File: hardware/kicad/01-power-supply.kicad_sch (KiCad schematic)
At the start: 8 parts, among them J1 USB_C, U2 IP5306 USB-C, U3 AMS1117-3.3

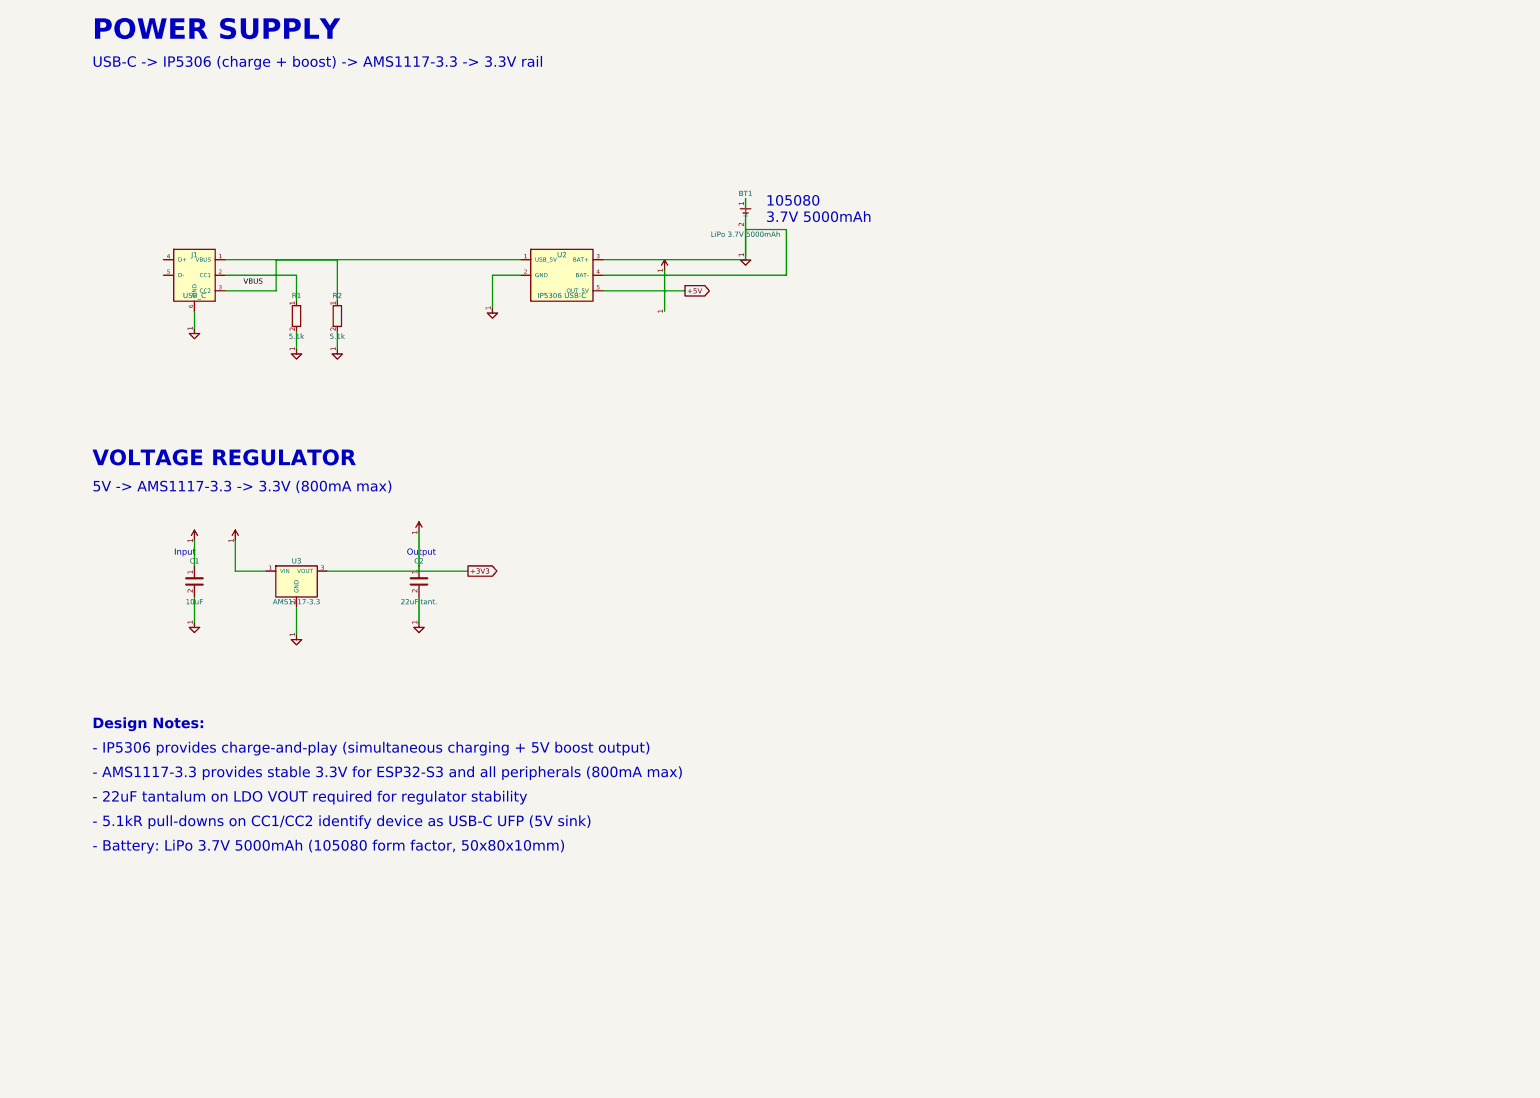
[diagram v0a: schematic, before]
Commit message: Add PCB layout, hierarchical schematics, verification & rendering pipeline
- Reorganize passive components into centered rows below ESP32
- Add missing schematic symbols (LED, FPC_16P, SW_PWR, SW13, SPK1)
- Generate hierarchical root schematic with 7 sub-sheet references
- Create PCB layout generator (4-layer, 160x75mm, JLCPCB-ready)
- Add JLCPCB export (BOM.csv + CPL.csv for 65 components)
- Add schematic/PCB/JLCPCB consistency verification script
- Add PCB SVG renderer + PNG/GIF animation pipeline
- Add interactive 3D PCB viewer (Three.js)
- Update docs (pcb.md, components.md, README.md)

Co-Authored-By: Claude Opus 4.6 <noreply@anthropic.com>
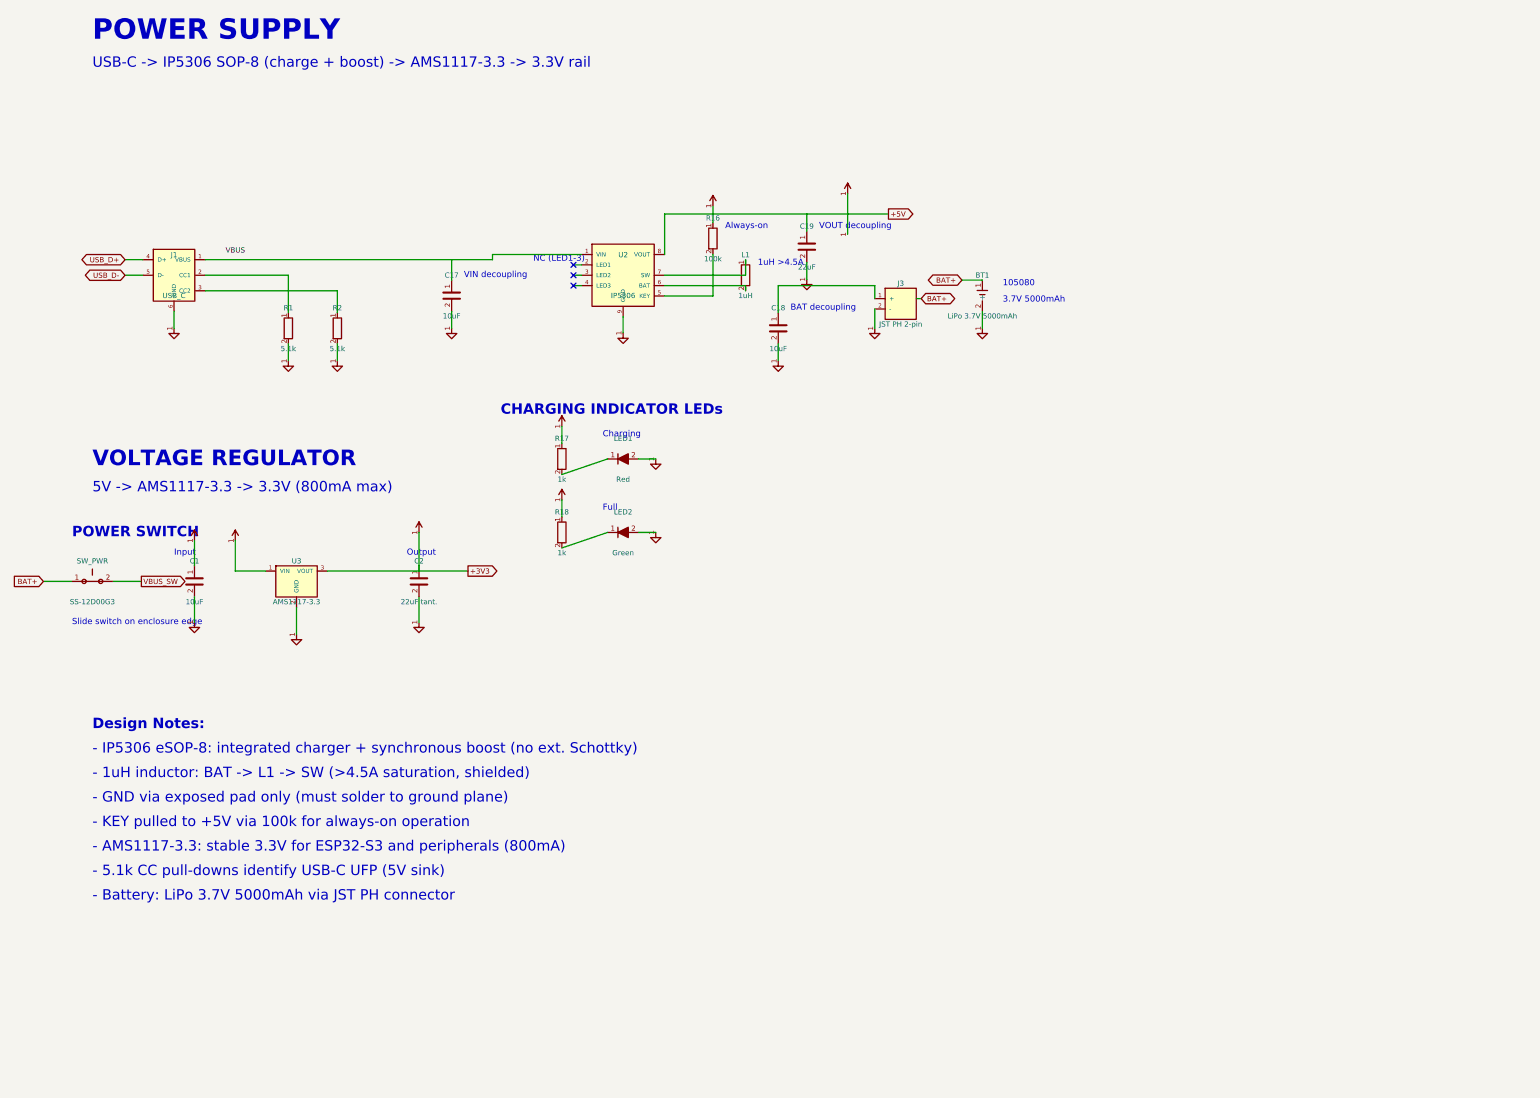
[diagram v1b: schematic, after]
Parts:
- added C17, C18: 10uF, symbol C
- added C19: 22uF, symbol C
- added J3: JST PH 2-pin, symbol Conn_JST_PH_2
- added L1: 1uH, symbol L
- added LED1: Red, symbol LED
- added LED2: Green, symbol LED
- added R16: 100k, symbol R
- added R17, R18: 1k, symbol R
- added SW_PWR: SS-12D00G3, symbol SW_Push
- U2: value IP5306 USB-C -> IP5306; symbol IP5306_Module -> IP5306
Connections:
- net +5V: now also U2.8 (VOUT); no longer U2.5 (OUT_5V)
- net at J1.1 (VBUS), U2.1 (VIN): now also C17.1; no longer J1.3 (CC2), R2.1
- net USB_D+: now reaches J1.4 (D+)
- net USB_D-: now reaches J1.5 (D-)
- new net: J1.3 (CC2), R2.1
- new net: R16.2, U2.5 (KEY)
- new net: L1.2, U2.6 (BAT)
- new net: L1.1, U2.7 (SW)
- new net: C18.1, J3.1 (+)
- new net: LED1.1 (A), R17.2
- new net: LED2.1 (A), R18.2
- new net BAT+: BT1.1 (+), SW_PWR.1
- new net VBUS_SW: SW_PWR.2
- now unconnected: BT1.2 (-), U2.3 (BAT+), U2.4 (BAT-)
- no-connect marks 0 -> 3
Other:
- note added: "- 1uH inductor: BAT -> L1 -> SW (>4.5A saturation, shielded)"
- note added: "- 5.1k CC pull-downs identify USB-C UFP (5V sink)"
- note added: "- AMS1117-3.3: stable 3.3V for ESP32-S3 and peripherals (800mA)"
- note added: "- Battery: LiPo 3.7V 5000mAh via JST PH connector"
- note added: "- GND via exposed pad only (must solder to ground plane)"
- note added: "- IP5306 eSOP-8: integrated charger + synchronous boost (no ext. Schottky)"
- note added: "- KEY pulled to +5V via 100k for always-on operation"
- note added: "1uH >4.5A"
- note added: "Always-on"
- note added: "BAT decoupling"
- note added: "CHARGING INDICATOR LEDs"
- note added: "Charging"
- note added: "Full"
- note added: "NC (LED1-3)"
- note added: "POWER SWITCH"
- note added: "Slide switch on enclosure edge"
- note added: "USB-C -> IP5306 SOP-8 (charge + boost) -> AMS1117-3.3 -> 3.3V rail"
- note added: "VIN decoupling"
- note added: "VOUT decoupling"
- note removed: "- 22uF tantalum on LDO VOUT required for regulator stability"
- note removed: "- 5.1kR pull-downs on CC1/CC2 identify device as USB-C UFP (5V sink)"
- note removed: "- AMS1117-3.3 provides stable 3.3V for ESP32-S3 and all peripherals (800mA max)"
- note removed: "- Battery: LiPo 3.7V 5000mAh (105080 form factor, 50x80x10mm)"
- note removed: "- IP5306 provides charge-and-play (simultaneous charging + 5V boost output)"
- note removed: "USB-C -> IP5306 (charge + boost) -> AMS1117-3.3 -> 3.3V rail"
- moved on the sheet: J1

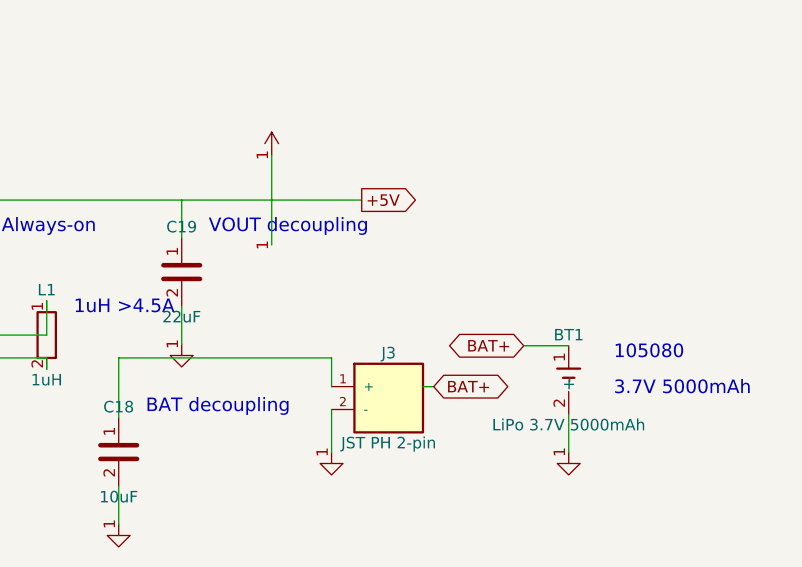
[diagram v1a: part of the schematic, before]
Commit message: feat(pcb): add bypass caps C26/C27, fix USB D+/D- matching, improve DRC/connectivity checks
- Add C26 (100nF VDD bypass near ESP32 pin 2) and C27 (10uF HF decoupling near AMS1117)
- Fix USB D+/D- length mismatch: 5-loop meander (0.46mm amp) reduces delta from 1.75mm to 0.03mm
- Fix LCD_RD/LCD_BL traces to use correct net IDs instead of +3V3
- Improve net connectivity check: count vias, allow stub-to-via patterns, exclude I2S unrouted nets
- Rewrite FPC/ESP32 pin position tests to use routing._PADS as source of truth
- Add Quantity column to BOM for JLCPCB assembly quoting
- Reduce min via hole size 0.3mm→0.2mm in design rules
- All 149 DFM/DFA/JLCPCB tests pass, 0 collisions

Co-Authored-By: Claude Opus 4.6 (1M context) <noreply@anthropic.com>
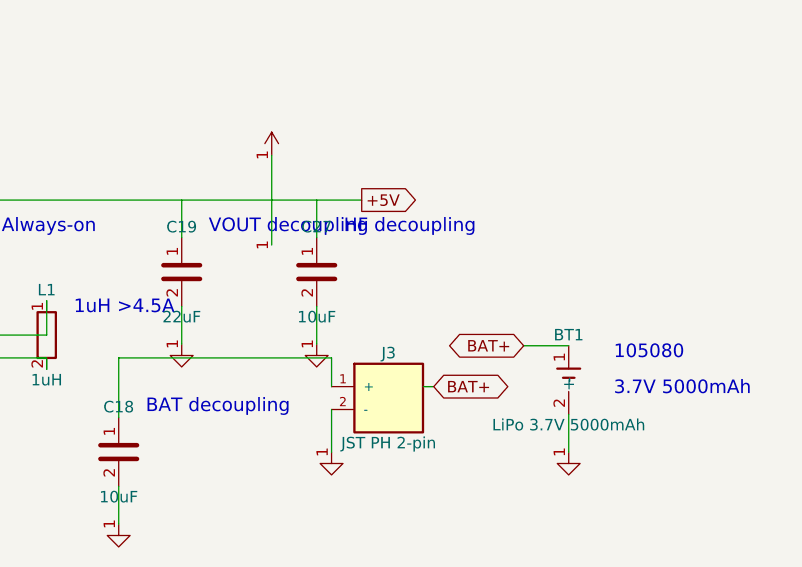
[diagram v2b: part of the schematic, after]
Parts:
- removed C18: 10uF, symbol C
- removed SW_PWR: SS-12D00G3, symbol SW_Push
- added C27: 10uF, symbol C
- added R16: 100k, symbol R
- added R17: 1k, symbol R
- C18: renamed from R16; value 100k -> 10uF; symbol R -> C
- SW_PWR: renamed from R17; value 1k -> SS-12D00G3; symbol R -> SW_Push
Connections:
- net BAT+: now also SW_PWR.1
- net VBUS_SW: now also SW_PWR.2
- net at U2.5 (KEY): now also R16.2; no longer C18.2
- net at J3.1 (+): now also C18.1
- net at LED1.1 (A): now also R17.2; no longer SW_PWR.2
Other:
- note added: "HF decoupling"

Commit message: fix(hw): R4 audit — schematic↔PCB sync guard + 4 fixes + R4-CRIT-1 false-positive closure
Round 4 of the hardware audit found four real schematic/PCB drift bugs
that rounds 1-3 missed because no check cross-validated the two Python
generators. A fifth finding (R4-CRIT-1, "FPC pinout mismatch") turned
out to be a FALSE POSITIVE caused by the landscape FPC pin reversal
(connector_pad = 41 − panel_pin) — verified programmatically against
all 40 J4 pads of the panel datasheet in components.md.

Fixes applied:
  R4-HIGH-1  USBLC6 (U4) + R22/R23 instantiated in power_supply.py —
             previously only in routing.py, invisible to schematic
             review.
  R4-HIGH-2  Display module symbol ref renamed U4 → DS1 in display.py.
             U4 is now cleanly owned by the physical USBLC6 TVS.
  R4-HIGH-3  PAM8403 R20/R21 input bias moved from GND to VREF
             (pin 8) per the datasheet single-ended app circuit.
  R4-CRIT-1  CLOSED as false positive. Both display.py (panel-side)
             and datasheet_specs.py (connector-side) were correct all
             along. Added 41-N reversal documentation at the top of
             both files so the mistake can't be re-raised.
  ERC CRIT   Pre-existing "Power output ↔ Power output" on +5V was
             PWR_FLAG duplicating IP5306 VOUT (already power_out in the
             library symbol). Removed the PWR_FLAG. ERC now 0 critical.

Incidental cleanups required by the new sync guard:
  - mcu.py R3 (external EN pull-up) removed from schematic — already
    DNP in BOM because the WROOM-1 module has an internal pull-up.
  - controls.py D1 BAT54C (MENU combo diode) instantiated in schematic
    to match the PCB routing. MENU button wiring simplified to the
    MENU_K node; there is no dedicated BTN_MENU GPIO (firmware detects
    START+SELECT combo).
  - power_supply.py USB_CC1 / USB_CC2 global labels added so the
    connector-net coverage check sees the full USB-C net set.
  - display.py docstring expanded with the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
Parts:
- removed C18: 10uF, symbol C
- removed C2: 22uF tant., symbol C
- added R1: 5.1k, symbol R
- added R18: 1k, symbol R
- added R22, R23: 22, symbol R
- added SW_PWR: SS-12D00G3, symbol SW_Push
- C1: renamed from SW_PWR; value SS-12D00G3 -> 10uF; symbol SW_Push -> C
- C2: renamed from R18; value 1k -> 22uF tant.; symbol R -> C
- U4: renamed from R1; value 5.1k -> USBLC6-2SC6; symbol R -> USBLC6_2SC6
- renumbered C1 to C18
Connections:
- net +3V3: now also C2.1
- net BAT+: now also SW_PWR.1; no longer C1.1
- net VBUS_SW: now also SW_PWR.2; no longer C1.2
- net USB_CC1: now reaches J1.2 (CC1)
- net USB_CC1: now also R1.1; no longer U4.1
- net USB_CC2: now reaches J1.3 (CC2), R2.1
- net at J3.1 (+): now also C18.1
- net at C2.2: no longer LED2.1 (A)
- new net: LED2.1 (A), R18.2
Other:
- note added: "D+ 22Ω"
- note added: "D- 22Ω"
- note added: "USB ESD TVS"
- moved on the sheet: C18

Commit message: docs+sch(review): schematic review — SW_PWR not in series (v1), broken PDF links, 6-sheet cleanup
Full review of schematics vs PCB/BOM/docs, triggered by the broken
https://pjcau.github.io/img/schematics/01-power-supply.pdf link.

Critical finding — SW_PWR cannot power off the v1 board:
only the switch common pin (pad 2) is routed, as a BAT+ stub; throw
pins 1/3 are unrouted (datasheet_specs declares them unconnected).
The battery path J3 -> Q1 -> BAT+ -> IP5306.6 is continuous copper.
- schematics.md: caution admonition, corrected power-path diagram
  (Q1/BAT_IN split included), flash procedure note (unplug J3 for
  true isolation), SW_PWR table row warning. v2 item: wire pins 1-2
  in series.
- power_supply.py sheet: removed stale VBUS_SW glabel (net exists
  nowhere), truthful switch drawing + as-built warning texts, actual
  part noted (MSK12C02 C431540; value string stays SS-12D00G3 to
  match CPL key).

Broken links (missing /esp32-emu-turbo/ baseUrl on raw JSX hrefs):
- schematics.md (7 PDF links), pcb.md (3D viewer), verification.md
  (2 DFM reports) — all now use useBaseUrl().
- Fixed 5 pre-existing broken anchors (phase-5 audio coprocessor
  links pointed at /docs/software instead of snes-optimization;
  one-rule admonition had no anchor).

Doc drift closed in schematics.md:
- Sheet 1 table: added U4 USBLC6, R22/R23 22R, Q1 SI2301, R24 100k,
  C27 10uF; sheet 2 table: added C26 VDD bypass.
- Backfeed table: reversed-battery row (Q1 body diode).
- v2 coprocessor sheet: decoupling refs renamed C28/C29 (C26/C27
  already used on main board).

Sheet 7 joystick was dead code (not in SHEET_DEFS since removal):
- deleted sheets/joystick.py, stale 07-joystick.kicad_sch and
  orphan 07-joystick.pdf; docs now say 6 sheets; regenerated all
  .kicad_sch + SVG/PDF renders; combined PDF rebuilt (6 pages).

Gates: verify_schematic_pcb_sync PASS; Docusaurus build clean
(0 broken links/anchors).

Co-Authored-By: Claude Fable 5 <noreply@anthropic.com>
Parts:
- added Q1: SI2301CDS, symbol BAT54C
- added R24: 100k, symbol R
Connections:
- net BAT+: no longer BT1.1 (+)
- net at C18.1: no longer J3.1 (+)
- net at J3.2 (-): now also J3.1 (+)
- net VBUS_SW: no longer names the net of SW_PWR.2
- new net BAT_IN: BT1.1 (+)
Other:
- note added: "!! v1 as-built: NOT in series - cannot disconnect battery"
- note added: "Actual part: MSK12C02 (LCSC C431540)"
- note added: "Gate pull-down"
- note added: "N.C. (v1: throw pins unrouted)"
- note added: "P-MOSFET RPP"
- note added: "Power on/off = IP5306 KEY + auto-standby. v2: wire pins 1-2 in series."
- note added: "SI2301CDS"
- note removed: "Slide switch on enclosure edge"

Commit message: sch(layout): fix annotation overlaps across all 6 sheets — reflow to A3 where needed
Root cause: multiple sheets had annotation text boxes placed too close
to each other or to component symbols/net labels. On the live website
this rendered as strings running through each other and through
component pins — unreadable in the schematic viewer.

Per-sheet fixes:

* Sheet 1 — Power Supply
  - Upgraded to A3 landscape (was A4). USB ESD (U4/R22/R23) had
    been placed at (45, 160) directly on top of SW_PWR, C1, U3
    and C2 — all at y=160. There was no room on A4 to fit both
    the input stage (USB-C + IP5306 + battery) and the output
    stage (AMS1117 + LEDs + power switch + USB ESD) with clean
    annotations.
  - USB ESD block relocated to its own dedicated row (y=140).
  - CHARGING INDICATOR LEDs moved to a dedicated right-side zone
    (x=275, y=145) so they no longer collide with USB ESD.
  - POWER SWITCH moved to its own right-side zone (x=285, y=200)
    so its long "v1 as-built" help text no longer crosses through
    C1 / U3 (AMS1117) / C2.
  - VOLTAGE REGULATOR title + AMS1117 area pushed down (y=175 /
    y=200) with DESIGN NOTES following (y=240).
  - C18 (BAT bypass) moved left of Q1, out of the "P-MOSFET RPP /
    SI2301CDS" label zone; C27 (HF bypass) spaced further from C19
    (was 15mm gap, now 22mm) so "VOUT bulk" label no longer runs
    into "HF bypass".
  - Q1 dual annotation stacked with 3mm vertical spacing (was 2mm).
  - R24 label moved BELOW its symbol as "Q1 gate PD".
  - J3 / BT1 pushed further right (jst_x=268, bt_x=315) to use A3
    width and clear the Q1 cluster.

* Sheet 2 — MCU (ESP32-S3)
  - EN pull-up annotation shortened + moved up so it no longer
    collides with the "RC reset delay" label below.
  - BOOT switch pushed further down (c_en_y + 55) and left of the
    RESET switch so its BTN_SELECT glabel and help text no longer
    overlap the DISPLAY / AUDIO / CONTROLS annotation column. Help
    text now sits below the switch in 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
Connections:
- net +5V: now also C19.1, C27.1
- net at L1.2, U2.6 (BAT): now also C18.1
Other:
- note added: "(SI2301CDS)"
- note added: "BAT bypass"
- note added: "HF bypass"
- note added: "Q1 gate PD"
- note added: "VOUT bulk"
- note removed: "BAT decoupling"
- note removed: "Gate pull-down"
- note removed: "HF decoupling"
- note removed: "SI2301CDS"
- note removed: "VOUT decoupling"
- moved on the sheet: C27, R22, R23
